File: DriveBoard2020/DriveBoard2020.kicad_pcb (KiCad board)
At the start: 2 copper layers, 125 x 175.3 mm, 88 parts, among them U1 MAX_3232, U2 MAX_3232, U3 OKI, U4 TM4C129E_Launchpad, U5 MAX_3232, U6 OKI, U8 LDD-1500L

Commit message: Changes from Review
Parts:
- added G***: LOGO, MRDT_Silkscreens:z_sig_Sam_Thompson_Sig_20.0mmX13.1mm, F.Cu at (197.6, 237.7)
- added G***: LOGO, DriveBoard_Hardware:z_sig_Jack_Schott_15.2mmx27mm, F.Cu at (184.9, 227.1)
- added G***: LOGO, DriveBoard_Hardware:z_sig_Jared_Sinkey_15.5mmx34.4mm, F.Cu at (217.4, 225.6)

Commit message: more layout changes
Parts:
- removed 3.3V, 5V: LED, LED_SMD:LED_0603_1608Metric_Pad1.05x0.95mm_HandSolder
- removed Conn11: Molex_SL_02, MRDT_Connectors:MOLEX_SL_02_Horizontal
- removed G***: LOGO, MRDT_Silkscreens:z_sig_Sam_Thompson_Sig_20.0mmX13.1mm
- removed G***: LOGO, DriveBoard_Hardware:z_sig_Jack_Schott_15.2mmx27mm
- removed G***: LOGO, DriveBoard_Hardware:z_sig_Jared_Sinkey_15.5mmx34.4mm
- added D16: LED, LED_SMD:LED_0603_1608Metric_Pad1.05x0.95mm_HandSolder, F.Cu at (212.3, 189.5)
- added D18: LED, LED_SMD:LED_0603_1608Metric_Pad1.05x0.95mm_HandSolder, F.Cu at (118.8, 201.9)
- added D7: LED, LED_SMD:LED_0603_1608Metric_Pad1.05x0.95mm_HandSolder, F.Cu at (218.1, 189.4)
- added R21: 500, Resistor_SMD:R_0603_1608Metric_Pad1.05x0.95mm_HandSolder, F.Cu at (118.7, 203.8)
- Conn9: value Molex_SL_02 -> Molex_SL_03; footprint MRDT_Connectors:MOLEX_SL_02_Horizontal -> MRDT_Connectors:MOLEX_SL_03_Horizontal
- R15: value 330 -> 10k
- R16, R17: value 500 -> 10k
- SW0: renamed from Switch Direction
- SW1: renamed from Front Right
- SW2: renamed from Front Left
- SW3: renamed from Middle Right
- SW4: renamed from Middle Left
- SW5: renamed from Rear Right
- SW6: renamed from Rear Left
- SW8: renamed from Neopixel White
- U4: footprint MRDT_Shields:TM4C129E_Launchpad_FULL_THT_BOTTOM -> MRDT_Shields:TM4C129E_Launchpad_FULL_SMD_BOTTOM
- moved R19 133.3 mm to (212.3, 191.3)
- moved R7 133.3 mm to (218.1, 191.3)
- moved SW0 103.8 mm to (120.8, 186.4), turned to 270 degrees
- moved D13 101.9 mm to (168.9, 210.3)
- moved D14 101.9 mm to (156.2, 210.3)
- moved R13 101.9 mm to (162.6, 210.3)
- moved R14 101.9 mm to (151.1, 210.3)
- moved SW3 101.9 mm to (166.0, 192.5)
- moved SW4 101.9 mm to (154.6, 192.5)
- moved SW6 101.9 mm to (154.6, 204.0)
- moved D10 101.9 mm to (156.2, 184.9)
- moved D11 101.9 mm to (168.9, 197.6)
- moved D12 101.9 mm to (156.2, 197.6)
- moved D9 101.9 mm to (168.9, 184.9)
- moved R10 101.9 mm to (151.1, 184.9)
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- renumbered Tx6 to D1, Tx7 to D15, Rx7 to D19, Rx6 to D2, Tx5 to D20, Rx5 to D21, Tx2 to D22, Rx2 to D23, Tx4 to D3, Rx4 to D4, Tx3 to D5, Rx3 to D6, Headlights to SW7, Neopixel to SW9
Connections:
- net clk2 renamed CLK2
- net cs2 renamed CS2
- Conn9 pad 1: Dout_NeoPixel -> +5V
- SW8 pad 1: +5V -> +3V3
- SW9 pad 1: +5V -> +3V3
- U4 pad PF2: Net-(U4-PadPF2) -> Dout_NeoPixel
- U4 pad PM6: switch_direction -> Switch_Direction
- U4 pad PP2: Dout_NeoPixel -> Net-(U4-PadPP2)
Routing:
- net +3V3: track 297.9 -> 0.00 mm, vias 4 -> 0
- net +5V: track 223.0 -> 0.00 mm, vias 3 -> 0
- net Rx2: track 216.0 -> 0.00 mm, vias 4 -> 0
- net Rx7: track 214.7 -> 0.00 mm, vias 6 -> 0
- net Tx7: track 211.6 -> 0.00 mm, vias 6 -> 0
- net FL_Motor: track 202.3 -> 0.00 mm, vias 4 -> 0
- net FR_Motor: track 198.9 -> 0.00 mm, vias 4 -> 0
- net Rx5: track 198.0 -> 0.00 mm, vias 3 -> 0
- net Tx5: track 193.2 -> 0.00 mm, vias 5 -> 0
- net NeoPixel_White: track 177.6 -> 0.00 mm, vias 4 -> 0
- net Rx3: track 175.1 -> 0.00 mm, vias 4 -> 0
- net Tx6: track 166.7 -> 0.00 mm, vias 3 -> 0
- net Tx3: track 166.5 -> 0.00 mm, vias 3 -> 0
- net Tx4: track 166.5 -> 0.00 mm, vias 6 -> 0
- net MR_Motor: track 164.1 -> 0.00 mm, vias 1 -> 0
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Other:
- outline, holes or cut-outs redrawn

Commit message: tentative layout/traces
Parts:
- moved D7 63.3 mm to (157.6, 170.6)
- moved R7 63.3 mm to (157.6, 172.5)
- moved D16 61.9 mm to (153.4, 170.7)
- moved R19 61.9 mm to (153.4, 172.5)
- moved C12 24.2 mm to (206.6, 163.6)
- moved U5 24.2 mm to (210.1, 157.2)
- moved C13 23.5 mm to (210.4, 163.6)
- moved C5 22.5 mm to (214.1, 163.6), turned to 180 degrees
- moved U2 16.0 mm to (142.2, 158.5)
- moved C3 15.7 mm to (145.7, 164.8)
- moved C7 15.2 mm to (141.7, 164.8)
- moved C6 14.4 mm to (137.8, 164.8)
- moved C1 13.7 mm to (218.4, 188.0), turned to 0 degrees
- moved C14 12.2 mm to (218.4, 190.5), turned to 0 degrees
- moved C15 6.37 mm to (208.8, 184.4), turned to 270 degrees
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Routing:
- net +3V3: track 0.00 -> 213.9 mm, vias 0 -> 4
- net +5V: track 0.00 -> 160.7 mm, vias 0 -> 7
- net Rx2: track 0.00 -> 158.6 mm, vias 0 -> 4
- net Rx5: track 0.00 -> 134.8 mm, vias 0 -> 3
- net Tx5: track 0.00 -> 133.0 mm, vias 0 -> 5
- net Headlight_OnOff_PWM: track 0.00 -> 118.4 mm, vias 0 -> 2
- net CS2: track 0.00 -> 118.0 mm, vias 0 -> 4
- net Tx6: track 0.00 -> 115.7 mm, vias 0 -> 5
- net CLK2: track 0.00 -> 109.1 mm, vias 0 -> 4
- net Rx6: track 0.00 -> 105.9 mm, vias 0 -> 3
- net Rx7: track 0.00 -> 98.0 mm, vias 0 -> 3
- net Tx7: track 0.00 -> 95.0 mm, vias 0 -> 4
- net Net-(Conn10-Pad2): track 0.00 -> 90.0 mm, vias 0 -> 2
- net Net-(Conn10-Pad1): track 0.00 -> 85.6 mm, vias 0 -> 2
- net Tx3: track 0.00 -> 85.5 mm, vias 0 -> 5
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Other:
- board size 125 x 175.3 mm -> 124.5 x 113.7 mm
- board text removed: "MOTORS"
- board text removed: "Power Indicators"
- board text removed: "Serial Indicators"

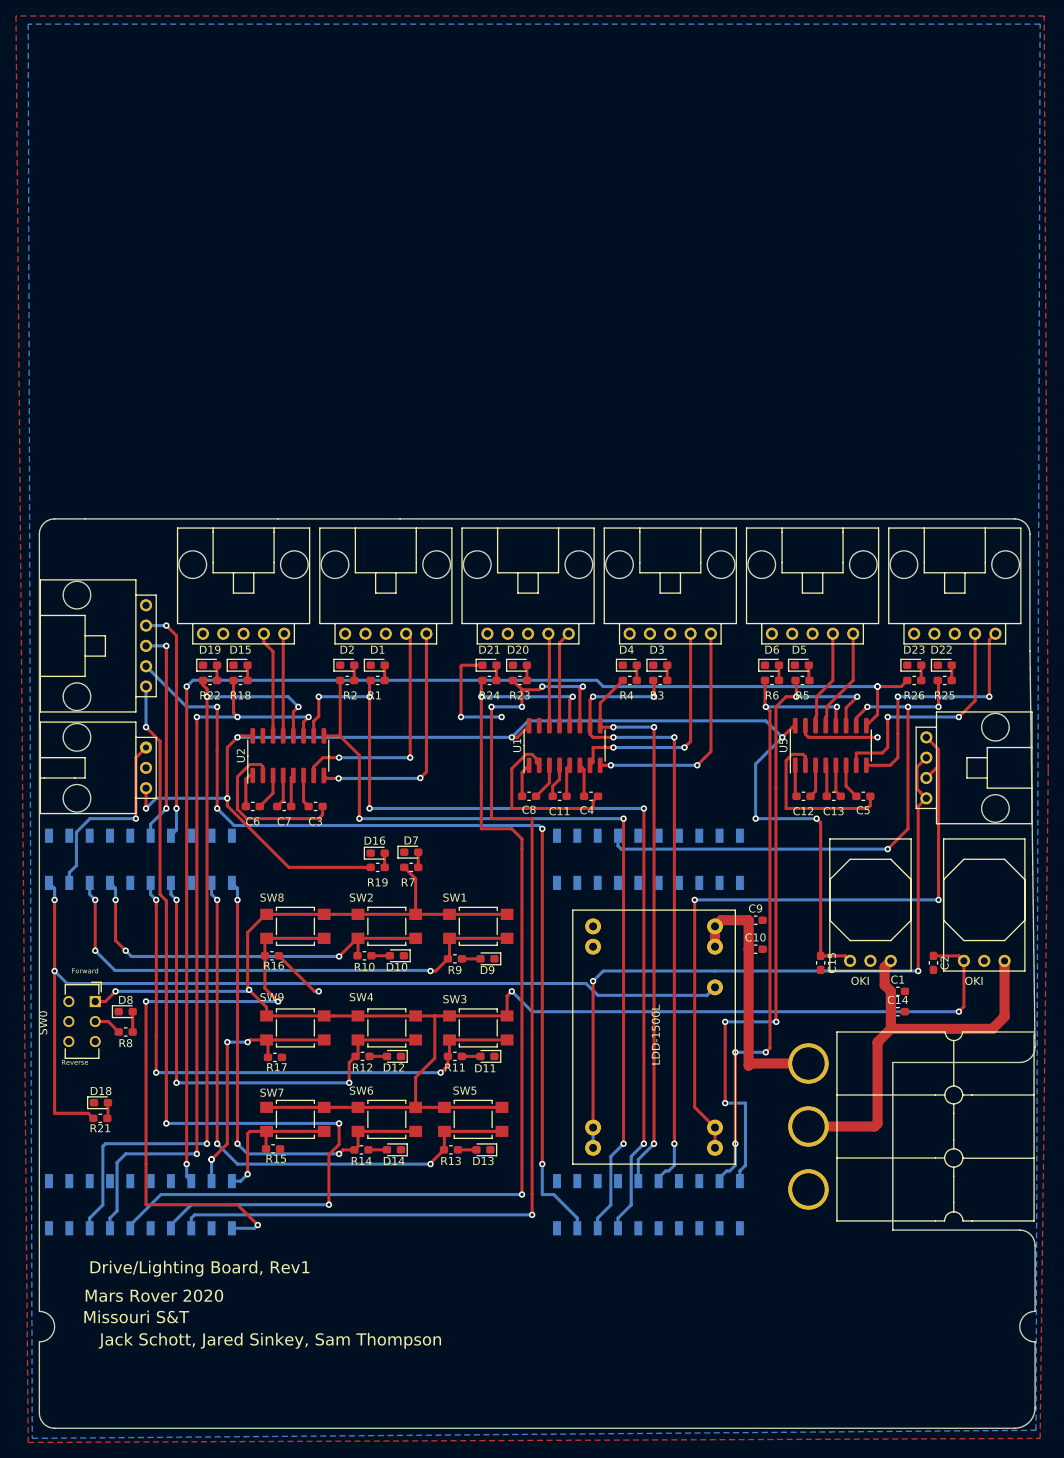
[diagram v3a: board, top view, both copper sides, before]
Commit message: silkscreens and via stitching, corrected some awful traces
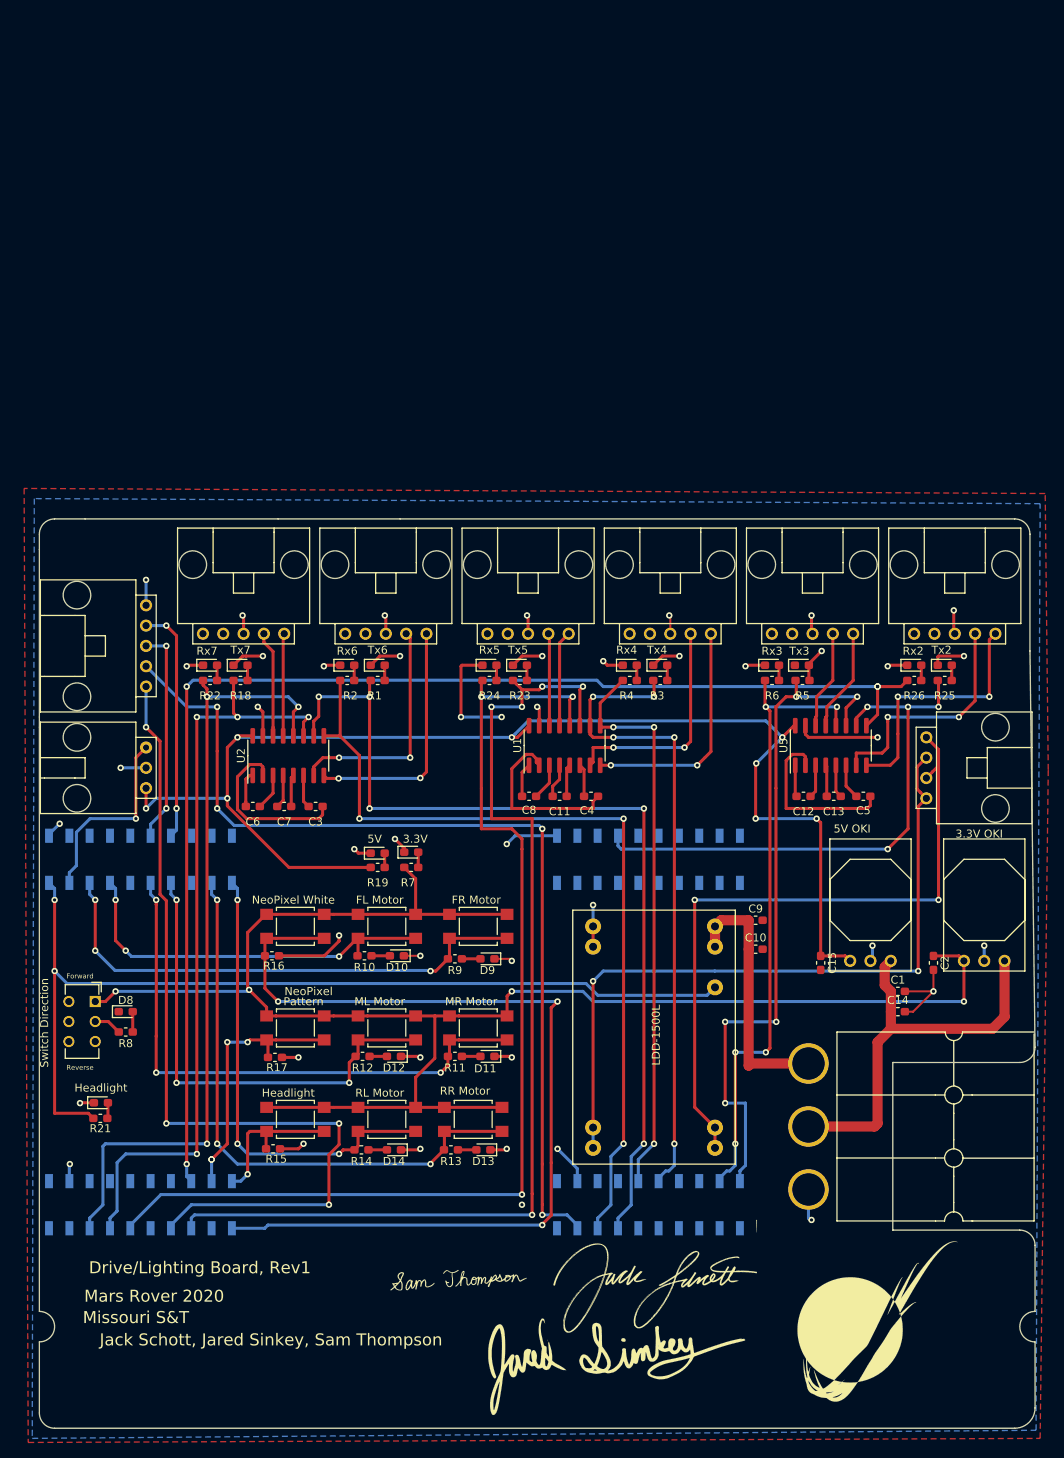
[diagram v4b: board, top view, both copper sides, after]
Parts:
- removed SW9: SW_Push, Button_Switch_SMD:SW_SPST_TL3305A
- added G***: LOGO, MRDT_Silkscreens:z_sig_Sam_Thompson_Sig_20.0mmX13.1mm, F.Cu at (163.2, 225.4)
- added G***: LOGO, DriveBoard_Hardware:z_sig_Jack_Schott_15.2mmx27mm, F.Cu at (187.3, 224.2)
- added G***: LOGO, DriveBoard_Hardware:z_sig_Jared_Sinkey_15.5mmx34.4mm, F.Cu at (183.5, 234.3)
- added G***: LOGO, MRDT_Silkscreens:0_MRDT_Logo_20mm, F.Cu at (215.9, 229.2)
- added Pattern: SW_Push, Button_Switch_SMD:SW_SPST_TL3305A, F.Cu at (143.1, 192.5)
- FL Motor: renamed from SW2
- FR Motor: renamed from SW1
- ML Motor: renamed from SW4
- MR Motor: renamed from SW3
- NeoPixel White: renamed from SW8
- RL Motor: renamed from SW6
- RR Motor: renamed from SW5
- Switch Direction: renamed from SW0
- U3: value OKI -> 3.3V OKI
- U6: value OKI -> 5V OKI
- renumbered D7 to 3.3V, D16 to 5V, SW7 to Headlight, D18 to Headlight, D23 to Rx2, D6 to Rx3, D4 to Rx4, D21 to Rx5, D2 to Rx6, D19 to Rx7, D22 to Tx2, D5 to Tx3, D3 to Tx4, D20 to Tx5, D1 to Tx6, D15 to Tx7
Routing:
- net GND: track 31.2 -> 158.4 mm, vias 4 -> 45
- net NeoPixel_White: track 76.2 -> 118.5 mm
- net Net-(D5-Pad2): track 1.94 -> 4.38 mm, vias 0 -> 1
- net +3V3: track 213.9 -> 212.5 mm
- net CS2: track 118.0 -> 119.0 mm
- net +5V: vias 7 -> 8
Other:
- board text added: "NeoPixel"

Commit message: corrected a few more traces
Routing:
- net Net-(C3-Pad1): track 21.4 -> 12.0 mm, vias 0 -> 2
- net Net-(C5-Pad1): track 21.8 -> 12.3 mm, vias 0 -> 2
- net Net-(C4-Pad1): track 21.9 -> 13.4 mm, vias 0 -> 2
- net Tx2: track 69.2 -> 70.6 mm
- net Rx5: track 134.8 -> 135.5 mm, vias 3 -> 5
- net Tx5: track 133.0 -> 133.8 mm, vias 5 -> 7
- net Tx3: vias 5 -> 7
- net GND: vias 45 -> 44
